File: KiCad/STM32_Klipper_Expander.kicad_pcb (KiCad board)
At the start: 2 copper layers, 100 x 24 mm, 47 parts, among them J1 USB_B_Micro, J10 Conn_01x01, J11 Conn_01x03, J12 Conn_01x02, J2 Conn_01x04, J4 Conn_01x03, J5 Vin, J6 Screw_Terminal_01x08, J7 Conn_01x02, J8 Conn_01x02, J9 Conn_01x02, Q1 IRLML6344TRPBF, Q2 IRLML6344TRPBF, Q3 IRLML6344TRPBF, Q4 IRLML6344TRPBF, SW2 SW_SPST, U1 STM32F042F6Px, U2 AP2127K-3.3, U3 74LVC1G17

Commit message: Addition of Interactive BOM
Interactive BOM courtesy of https://github.com/openscopeproject/InteractiveHtmlBom/
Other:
- board text added: "+ -"
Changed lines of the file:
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@@
   (general
     (thickness 1.6)
-    (drawings 35)
+    (drawings 36)
     (tracks 362)
     (zones 0)
@@
     )
   )
+  (gr_text "+   -" (at 161.422 88.819) (layer F.SilkS)
+    (effects (font (size 2 2) (thickness 0.3)))
+  )
   (gr_text "Klipper Expansion Board\nTimothy Abraham" (at 125.5 91.25) (layer B.SilkS)

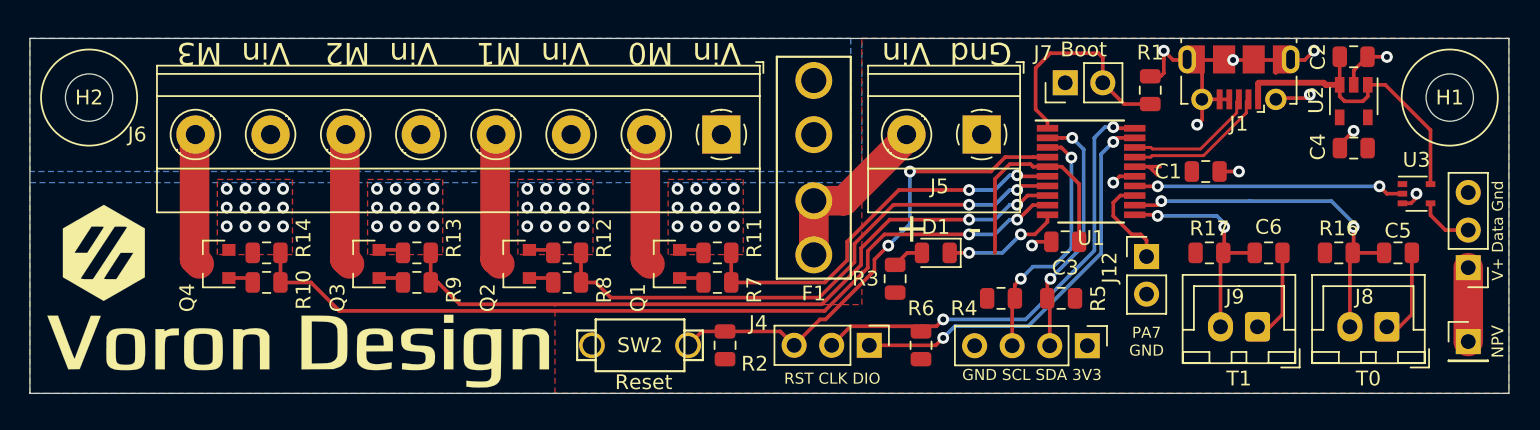
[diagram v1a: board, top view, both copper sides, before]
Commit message: Klipper Expander V2
Update to Klipper Expander that adds status LED's to the 4 mosfet outputs, 5V rail, and Vin rail.
Also changed 2 capacitors to use the same 4.7uF that are already present lowering the unique part count.
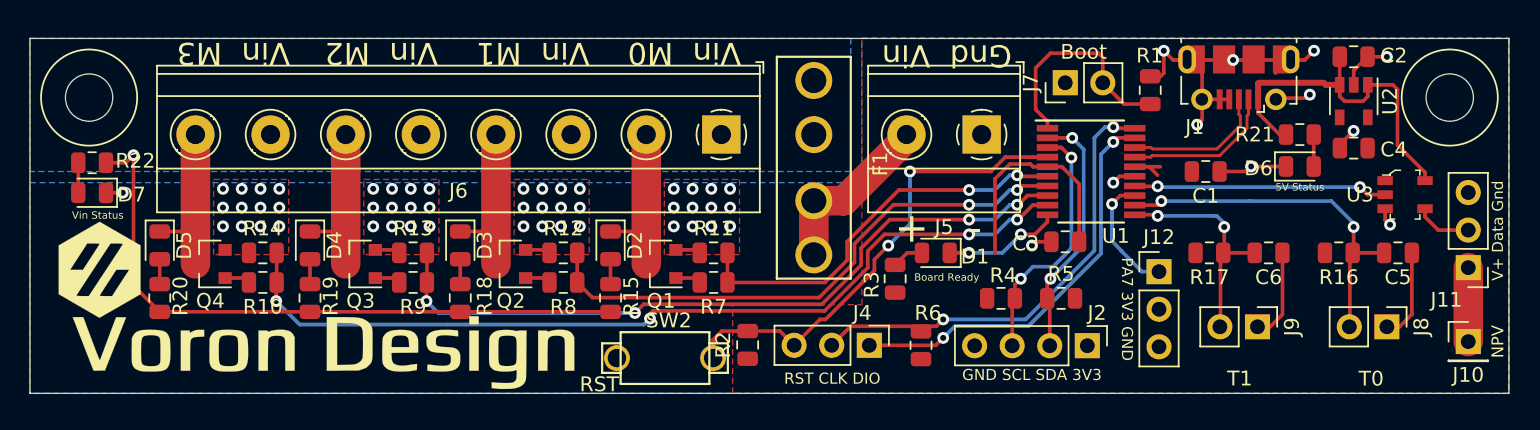
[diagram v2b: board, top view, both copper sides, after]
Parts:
- added D2: LED, KlipperExpander:LED_0805_2012Metric, F.Cu at (139.3, 90.0)
- added D3: LED, KlipperExpander:LED_0805_2012Metric, F.Cu at (129.1, 90.0)
- added D4: LED, KlipperExpander:LED_0805_2012Metric, F.Cu at (118.9, 90.0)
- added D5: LED, KlipperExpander:LED_0805_2012Metric, F.Cu at (108.8, 90.0)
- added D6: LED, KlipperExpander:LED_0805_2012Metric, F.Cu at (185.9, 84.7)
- added D7: LED, KlipperExpander:LED_0805_2012Metric, F.Cu at (104.2, 86.4)
- added R15: 4.7K, KlipperExpander:R_0805_2012Metric, F.Cu at (139.3, 93.5)
- added R18: 4.7K, KlipperExpander:R_0805_2012Metric, F.Cu at (129.1, 93.5)
- added R19: 4.7K, KlipperExpander:R_0805_2012Metric, F.Cu at (118.9, 93.5)
- added R20: 4.7K, KlipperExpander:R_0805_2012Metric, F.Cu at (108.8, 93.5)
- added R21: 1K, KlipperExpander:R_0805_2012Metric, F.Cu at (185.9, 82.5)
- added R22: 4.7K, KlipperExpander:R_0805_2012Metric, F.Cu at (104.2, 84.4)
- C1, C2, C3, C4: footprint Capacitor_SMD:C_0805_2012Metric -> KlipperExpander:C_0805_2012Metric
- C5, C6: value 10uF -> 4.7uF; footprint Capacitor_SMD:C_0805_2012Metric -> KlipperExpander:C_0805_2012Metric
- D1: footprint LED_SMD:LED_0805_2012Metric -> KlipperExpander:LED_0805_2012Metric
- F1: footprint TRA_KiCad_Footprints:3544-2_FuseHolder -> KlipperExpander:3544-2_FuseHolder
- H1, H2: footprint MountingHole:MountingHole_3.2mm_M3 -> KlipperExpander:MountingHole_3.2mm_M3
- J1: footprint TRA_KiCad_Footprints:Molex-105017-0001-USBMicroB -> KlipperExpander:Molex-105017-0001-USBMicroB
- J10: footprint Connector_PinHeader_2.54mm:PinHeader_1x01_P2.54mm_Vertical -> KlipperExpander:PinHeader_1x01_P2.54mm_Vertical
- J11, J4: footprint Connector_PinHeader_2.54mm:PinHeader_1x03_P2.54mm_Vertical -> KlipperExpander:PinHeader_1x03_P2.54mm_Vertical
- J12: value Conn_01x02 -> Conn_01x03; footprint Connector_PinHeader_2.54mm:PinHeader_1x02_P2.54mm_Vertical -> KlipperExpander:PinHeader_1x03_P2.54mm_Vertical
- J2: footprint Connector_PinHeader_2.54mm:PinHeader_1x04_P2.54mm_Vertical -> KlipperExpander:PinHeader_1x04_P2.54mm_Vertical
- J5: footprint TRA_KiCad_Footprints:1x02_ScrewTerminal_Phoenix -> KlipperExpander:1x02_ScrewTerminal_Phoenix
- J6: footprint TRA_KiCad_Footprints:TerminalBlock_Phoenix_MKDS-1,5-8-5.08_1x08_P5.08mm_Horizontal -> KlipperExpander:1x08_ScrewTerminal_Phoenix
- J7: footprint Connector_PinHeader_2.54mm:PinHeader_1x02_P2.54mm_Vertical -> KlipperExpander:PinHeader_1x02_P2.54mm_Vertical
- J8, J9: footprint Connector_JST:JST_XH_B02B-XH-A_1x02_P2.50mm_Vertical -> KlipperExpander:PinHeader_1x02_P2.54mm_Vertical
- Q1, Q2, Q3, Q4: footprint Package_TO_SOT_SMD:SOT-23 -> KlipperExpander:SOT-23
- R1, R10, R11, R12, R13, R14, R2, R3, R4, R5, R6, R7, R8, R9: footprint Resistor_SMD:R_0805_2012Metric -> KlipperExpander:R_0805_2012Metric
- R16, R17: value 10K -> 4.7K; footprint Resistor_SMD:R_0805_2012Metric -> KlipperExpander:R_0805_2012Metric
- SW2: footprint TRA_KiCad_Footprints:2PinTactileButton -> KlipperExpander:2PinTactileButton
- U1: footprint Package_SO:TSSOP-20_4.4x6.5mm_P0.65mm -> KlipperExpander:TSSOP-20_4.4x6.5mm_P0.65mm
- U2: footprint Package_TO_SOT_SMD:SOT-23-5 -> KlipperExpander:SOT-23-5
- U3: footprint Package_TO_SOT_SMD:SOT-353_SC-70-5 -> KlipperExpander:SOT-753
- moved SW2 1.90 mm to (142.9, 97.6)
- moved G*** 1.71 mm to (120.0, 96.6)
- moved R2 1.53 mm to (148.5, 96.7)
- moved J12 1.32 mm to (176.3, 91.8)
- moved G*** 1.18 mm to (104.7, 91.6)
- moved U3 0.77 mm to (193.0, 86.6), turned to 270 degrees
- moved Q1 0.25 mm to (142.7, 91.2)
- moved Q2 0.25 mm to (132.5, 91.2)
- moved Q3 0.25 mm to (122.4, 91.2)
- moved Q4 0.25 mm to (112.2, 91.2)
- moved R10 0.25 mm to (115.7, 92.5)
- moved R14 0.25 mm to (115.7, 90.5), turned to 180 degrees
- moved R11 0.25 mm to (146.2, 90.5), turned to 180 degrees
- moved R12 0.25 mm to (136.1, 90.5), turned to 180 degrees
- moved R13 0.25 mm to (125.9, 90.5), turned to 180 degrees
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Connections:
- J12 pad 2: GND -> +3V3
- R11 pad 1: GND -> PWM0
- R11 pad 2: PWM0 -> GND
- R12 pad 1: GND -> PWM1
- R12 pad 2: PWM1 -> GND
- R13 pad 1: GND -> PWM2
- R13 pad 2: PWM2 -> GND
- R14 pad 1: GND -> PWM3
- R14 pad 2: PWM3 -> GND
- R16 pad 1: +3V3 -> T0
- R16 pad 2: T0 -> +3V3
- R17 pad 1: +3V3 -> T1
- R17 pad 2: T1 -> +3V3
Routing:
- net /Vin: track 0.00 -> 43.9 mm, vias 0 -> 1
- net GND: track 52.3 -> 56.6 mm, vias 59 -> 60
- net VCC: track 21.5 -> 24.7 mm
- net Net-(D6-Pad2): track 0.00 -> 2.16 mm
- net /Mosfet0: track 9.02 -> 11.2 mm
- net /Mosfet2: track 9.02 -> 11.2 mm
- net /Mosfet3: track 9.02 -> 11.2 mm
- net /Mosfet1: track 9.02 -> 11.2 mm
- net Net-(D7-Pad2): track 0.00 -> 2.03 mm
- net PWM3: track 58.3 -> 60.3 mm, vias 2 -> 4
- net GPIO: track 6.59 -> 8.33 mm, vias 0 -> 1
- net Net-(D5-Pad2): track 0.00 -> 1.68 mm
- net Net-(D4-Pad2): track 0.00 -> 1.68 mm
- net Net-(D3-Pad2): track 0.00 -> 1.68 mm
- net Net-(D2-Pad2): track 0.00 -> 1.68 mm
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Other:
- board text added: "5V Status"
- board text added: "Board Ready"
- board text added: "Klipper Expansion Board Vs Timothy Abraham"
- board text added: "PA7 3V3 GND"
- board text added: "PA7 3v3 Gnd"
- board text added: "RST"
- board text added: "Vin Status"
- board text removed: "Klipper Expansion Board Timothy Abraham"
- board text removed: "PA7 GND"
- board text removed: "PA7 Gnd"
- board text removed: "Reset"
